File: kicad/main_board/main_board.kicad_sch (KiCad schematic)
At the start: 39 parts, among them J1 mic+, J2 mic-, J3 XLR2, J4 XLR1, J5 XLR3, Q1 BC859C, Q2 BC859C, Q3 BC859C, Q4 BC849C, Q5 JFET

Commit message: kicad headers updated, small simulation updates
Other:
- company: Author: helixfoober -> Author: felhub
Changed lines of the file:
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@@
   (title_block
     (title "diy_mm")
-    (date "2022-02-03")
+    (date "2022-02-04")
     (rev "v02")
-    (company "Author: helixfoober")
+    (company "Author: felhub")
     (comment 1 "Reference 2: https://sound-au.com/articles/mic-electret.htm")
     (comment 2 "Reference 1: https://sound-au.com/project93.htm")

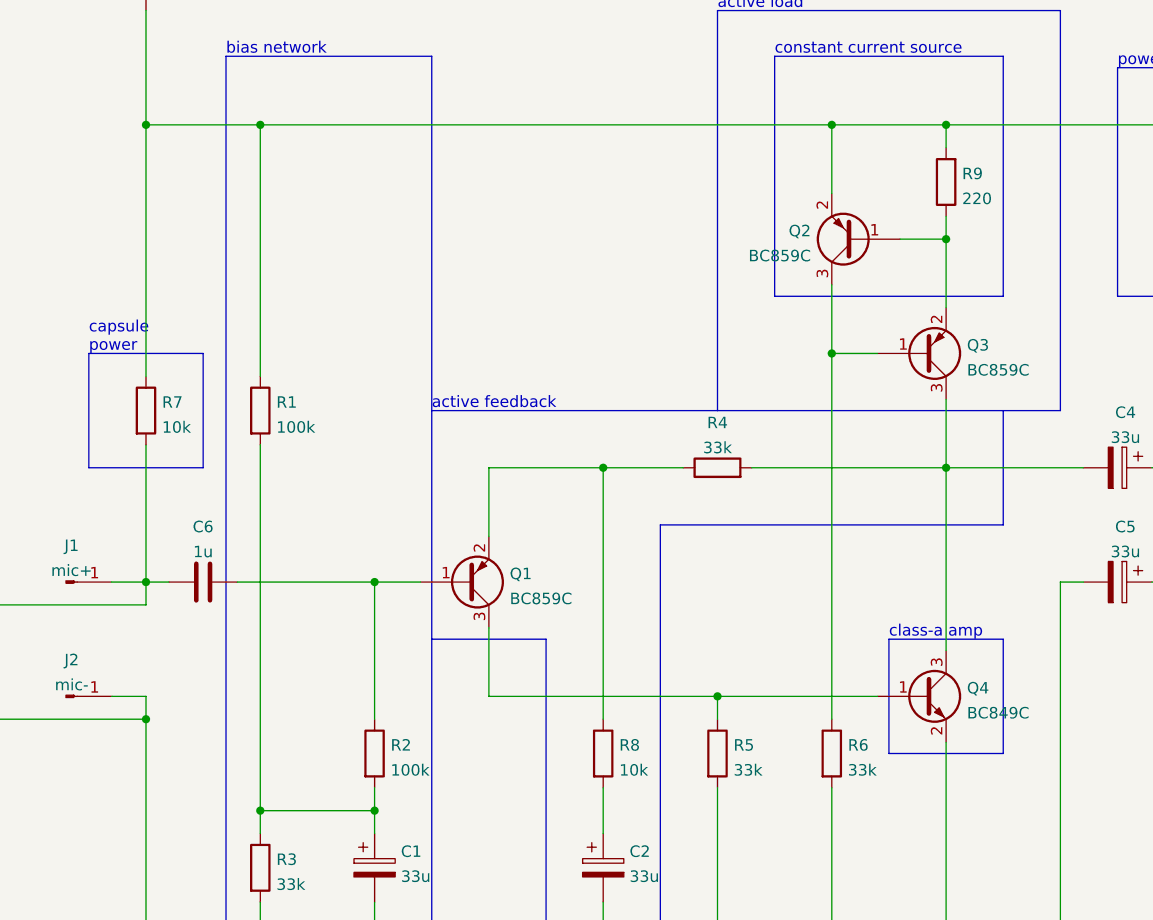
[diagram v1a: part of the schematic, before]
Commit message: new R labeling, capsule pwr 2.2k
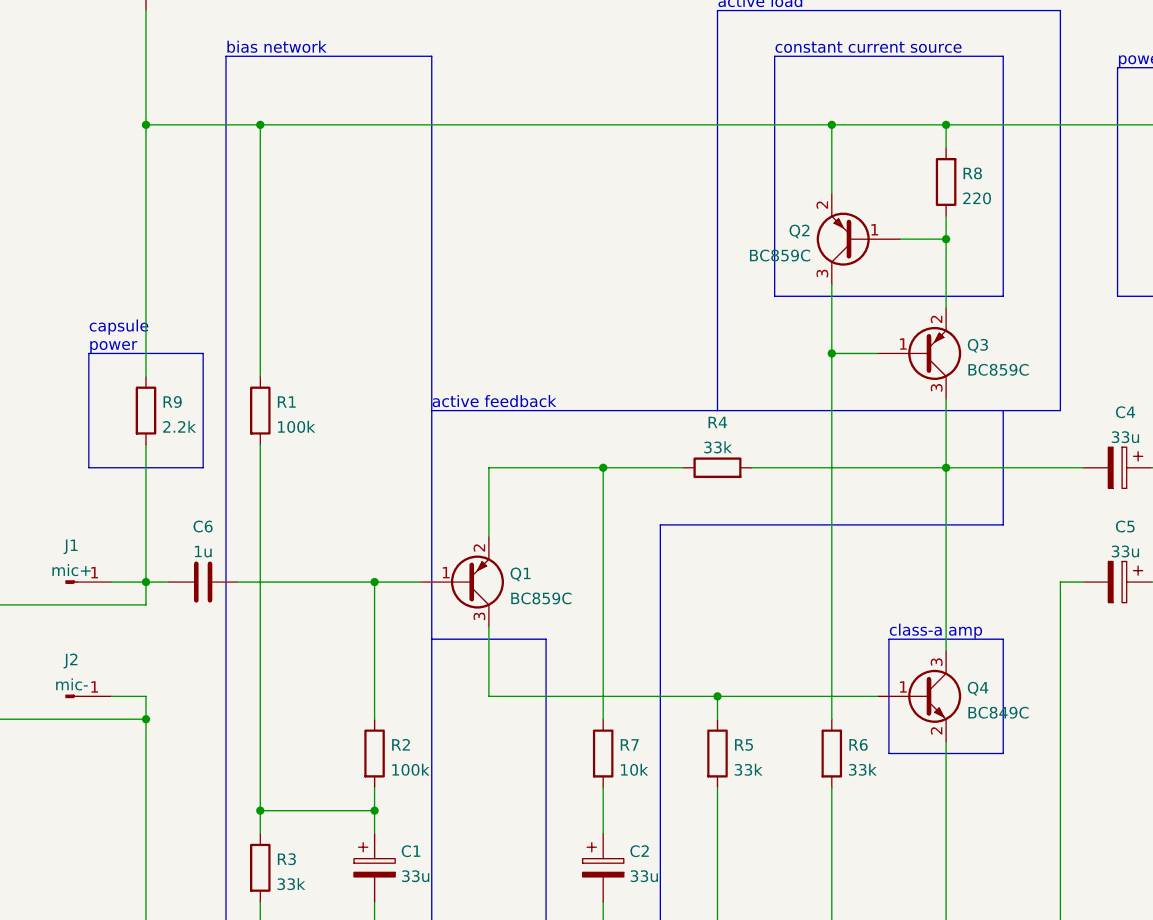
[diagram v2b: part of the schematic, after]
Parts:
- R9: renamed from R7; value 10k -> 2.2k
- renumbered R8 to R7, R9 to R8
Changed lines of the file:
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@@
   (symbol (lib_id "Device:R") (at 63.5 82.55 0) (unit 1)
     (in_bom yes) (on_board yes) (fields_autoplaced)
-    (property "Reference" "R7" (id 0) (at 65.278 81.6415 0)
-      (effects (font (size 1.27 1.27)) (justify left))
-    )
-    (property "Value" "10k" (id 1) (at 65.278 84.4166 0)
+    (property "Reference" "R9" (id 0) (at 65.278 81.6415 0)
+      (effects (font (size 1.27 1.27)) (justify left))
+    )
+    (property "Value" "2.2k" (id 1) (at 65.278 84.4166 0)
       (effects (font (size 1.27 1.27)) (justify left))
     )
@@
   (symbol (lib_id "Device:R") (at 114.3 120.65 0) (unit 1)
     (in_bom yes) (on_board yes) (fields_autoplaced)
-    (property "Reference" "R8" (id 0) (at 116.078 119.7415 0)
+    (property "Reference" "R7" (id 0) (at 116.078 119.7415 0)
       (effects (font (size 1.27 1.27)) (justify left))
     )
@@
   (symbol (lib_id "Device:R") (at 152.4 57.15 180) (unit 1)
     (in_bom yes) (on_board yes) (fields_autoplaced)
-    (property "Reference" "R9" (id 0) (at 154.178 56.2415 0)
+    (property "Reference" "R8" (id 0) (at 154.178 56.2415 0)
       (effects (font (size 1.27 1.27)) (justify right))
     )
@@
       (reference "R6") (unit 1) (value "33k") (footprint "Resistor_SMD:R_1206_3216Metric_Pad1.30x1.75mm_HandSolder")
     )
+    (path "/ebc0f200-aaaf-4fb3-9a8c-b05e9373ec3b"
+      (reference "R7") (unit 1) (value "10k") (footprint "Resistor_SMD:R_1206_3216Metric_Pad1.30x1.75mm_HandSolder")
+    )
+    (path "/fbd86f74-c842-4cef-a354-d7ac3f58ef35"
+      (reference "R8") (unit 1) (value "220") (footprint "Resistor_SMD:R_1206_3216Metric_Pad1.30x1.75mm_HandSolder")
+    )
     (path "/6615c595-191c-4fe5-b7e9-4a579d552656"
-      (reference "R7") (unit 1) (value "10k") (footprint "Resistor_SMD:R_1206_3216Metric_Pad1.30x1.75mm_HandSolder")
-    )
-    (path "/ebc0f200-aaaf-4fb3-9a8c-b05e9373ec3b"
-      (reference "R8") (unit 1) (value "10k") (footprint "Resistor_SMD:R_1206_3216Metric_Pad1.30x1.75mm_HandSolder")
-    )
-    (path "/fbd86f74-c842-4cef-a354-d7ac3f58ef35"
-      (reference "R9") (unit 1) (value "220") (footprint "Resistor_SMD:R_1206_3216Metric_Pad1.30x1.75mm_HandSolder")
+      (reference "R9") (unit 1) (value "2.2k") (footprint "Resistor_SMD:R_1206_3216Metric_Pad1.30x1.75mm_HandSolder")
     )
     (path "/d9604550-234a-4aad-a5db-f746ef7d25ac"

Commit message: small updates and new readme
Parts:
- D1: value 10V -> 9.1V
- R4: value 33k -> 10k
- renumbered R9 to R7, R7 to R8, R8 to R9
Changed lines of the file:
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@@
   (symbol (lib_id "Device:R") (at 63.5 82.55 0) (unit 1)
     (in_bom yes) (on_board yes) (fields_autoplaced)
-    (property "Reference" "R9" (id 0) (at 65.278 81.6415 0)
+    (property "Reference" "R7" (id 0) (at 65.278 81.6415 0)
       (effects (font (size 1.27 1.27)) (justify left))
     )
@@
     (in_bom yes) (on_board yes) (fields_autoplaced)
     (property "Reference" "R4" (id 0) (at 127 83.9175 90))
-    (property "Value" "33k" (id 1) (at 127 86.6926 90))
+    (property "Value" "10k" (id 1) (at 127 86.6926 90))
     (property "Footprint" "Resistor_SMD:R_1206_3216Metric_Pad1.30x1.75mm_HandSolder" (id 2) (at 127 90.678 90)
       (effects (font (size 1.27 1.27)) hide)
@@
       (effects (font (size 1.27 1.27)) (justify left))
     )
-    (property "Value" "10V" (id 1) (at 205.232 59.0166 90)
+    (property "Value" "9.1V" (id 1) (at 205.232 59.0166 90)
       (effects (font (size 1.27 1.27)) (justify left))
     )
@@
   (symbol (lib_id "Device:R") (at 114.3 120.65 0) (unit 1)
     (in_bom yes) (on_board yes) (fields_autoplaced)
-    (property "Reference" "R7" (id 0) (at 116.078 119.7415 0)
+    (property "Reference" "R8" (id 0) (at 116.078 119.7415 0)
       (effects (font (size 1.27 1.27)) (justify left))
     )
@@
   (symbol (lib_id "Device:R") (at 152.4 57.15 180) (unit 1)
     (in_bom yes) (on_board yes) (fields_autoplaced)
-    (property "Reference" "R8" (id 0) (at 154.178 56.2415 0)
+    (property "Reference" "R9" (id 0) (at 154.178 56.2415 0)
       (effects (font (size 1.27 1.27)) (justify right))
     )
@@
     )
     (path "/e1aef897-a92c-41c8-9bf2-bace864c8b2e"
-      (reference "D1") (unit 1) (value "10V") (footprint "Diode_SMD:D_MiniMELF")
+      (reference "D1") (unit 1) (value "9.1V") (footprint "Diode_SMD:D_MiniMELF")
     )
     (path "/522eef5b-59e9-42be-97d1-9a53b05e623d"
@@
     )
     (path "/723be6f5-ee0b-4b8e-a3d6-883e792c73f3"
-      (reference "R4") (unit 1) (value "33k") (footprint "Resistor_SMD:R_1206_3216Metric_Pad1.30x1.75mm_HandSolder")
+      (reference "R4") (unit 1) (value "10k") (footprint "Resistor_SMD:R_1206_3216Metric_Pad1.30x1.75mm_HandSolder")
     )
     (path "/fd35abb8-44e2-4fb3-90c9-d3362ff1067e"
@@
       (reference "R6") (unit 1) (value "33k") (footprint "Resistor_SMD:R_1206_3216Metric_Pad1.30x1.75mm_HandSolder")
     )
+    (path "/6615c595-191c-4fe5-b7e9-4a579d552656"
+      (reference "R7") (unit 1) (value "2.2k") (footprint "Resistor_SMD:R_1206_3216Metric_Pad1.30x1.75mm_HandSolder")
+    )
     (path "/ebc0f200-aaaf-4fb3-9a8c-b05e9373ec3b"
-      (reference "R7") (unit 1) (value "10k") (footprint "Resistor_SMD:R_1206_3216Metric_Pad1.30x1.75mm_HandSolder")
+      (reference "R8") (unit 1) (value "10k") (footprint "Resistor_SMD:R_1206_3216Metric_Pad1.30x1.75mm_HandSolder")
     )
     (path "/fbd86f74-c842-4cef-a354-d7ac3f58ef35"
-      (reference "R8") (unit 1) (value "220") (footprint "Resistor_SMD:R_1206_3216Metric_Pad1.30x1.75mm_HandSolder")
-    )
-    (path "/6615c595-191c-4fe5-b7e9-4a579d552656"
-      (reference "R9") (unit 1) (value "2.2k") (footprint "Resistor_SMD:R_1206_3216Metric_Pad1.30x1.75mm_HandSolder")
+      (reference "R9") (unit 1) (value "220") (footprint "Resistor_SMD:R_1206_3216Metric_Pad1.30x1.75mm_HandSolder")
     )
     (path "/d9604550-234a-4aad-a5db-f746ef7d25ac"
